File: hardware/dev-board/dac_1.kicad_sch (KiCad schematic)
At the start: 68 parts, among them IC1 ADV7393BCPZ, J2 CVBS

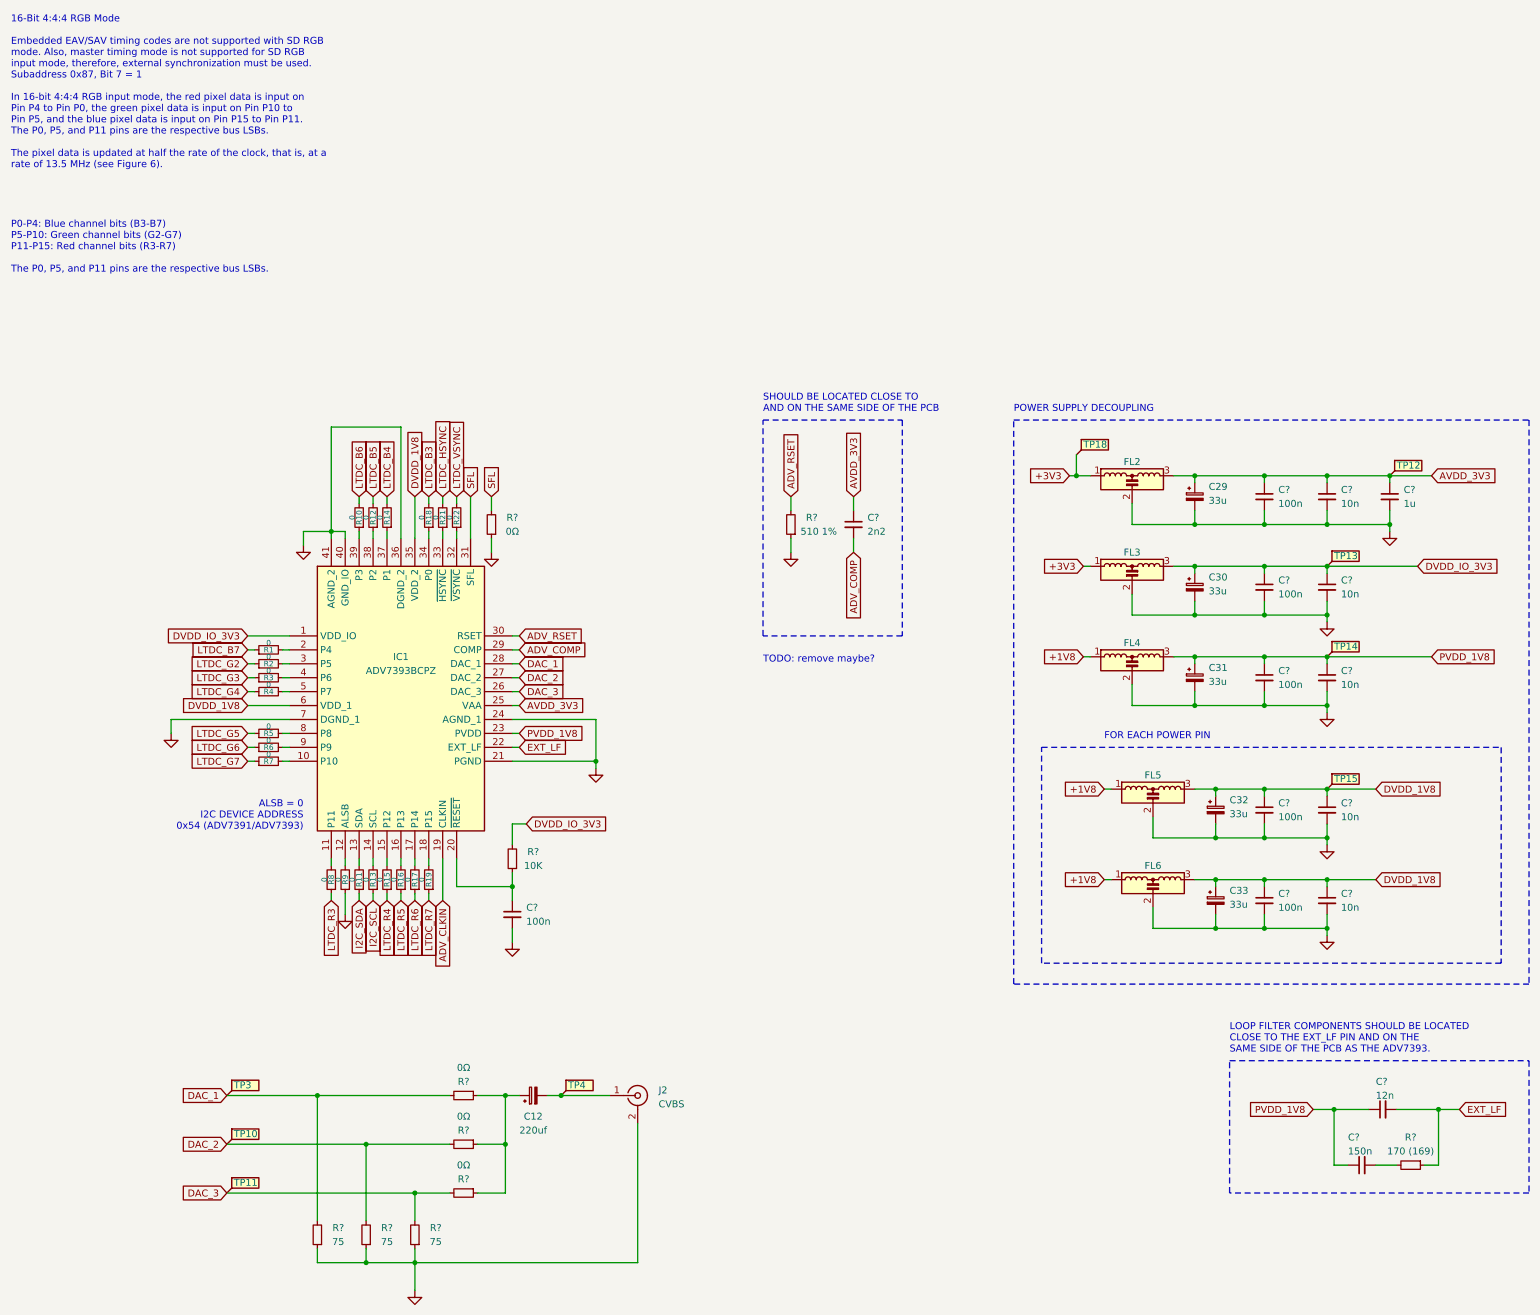
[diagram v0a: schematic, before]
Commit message: adv7393 dev-board done
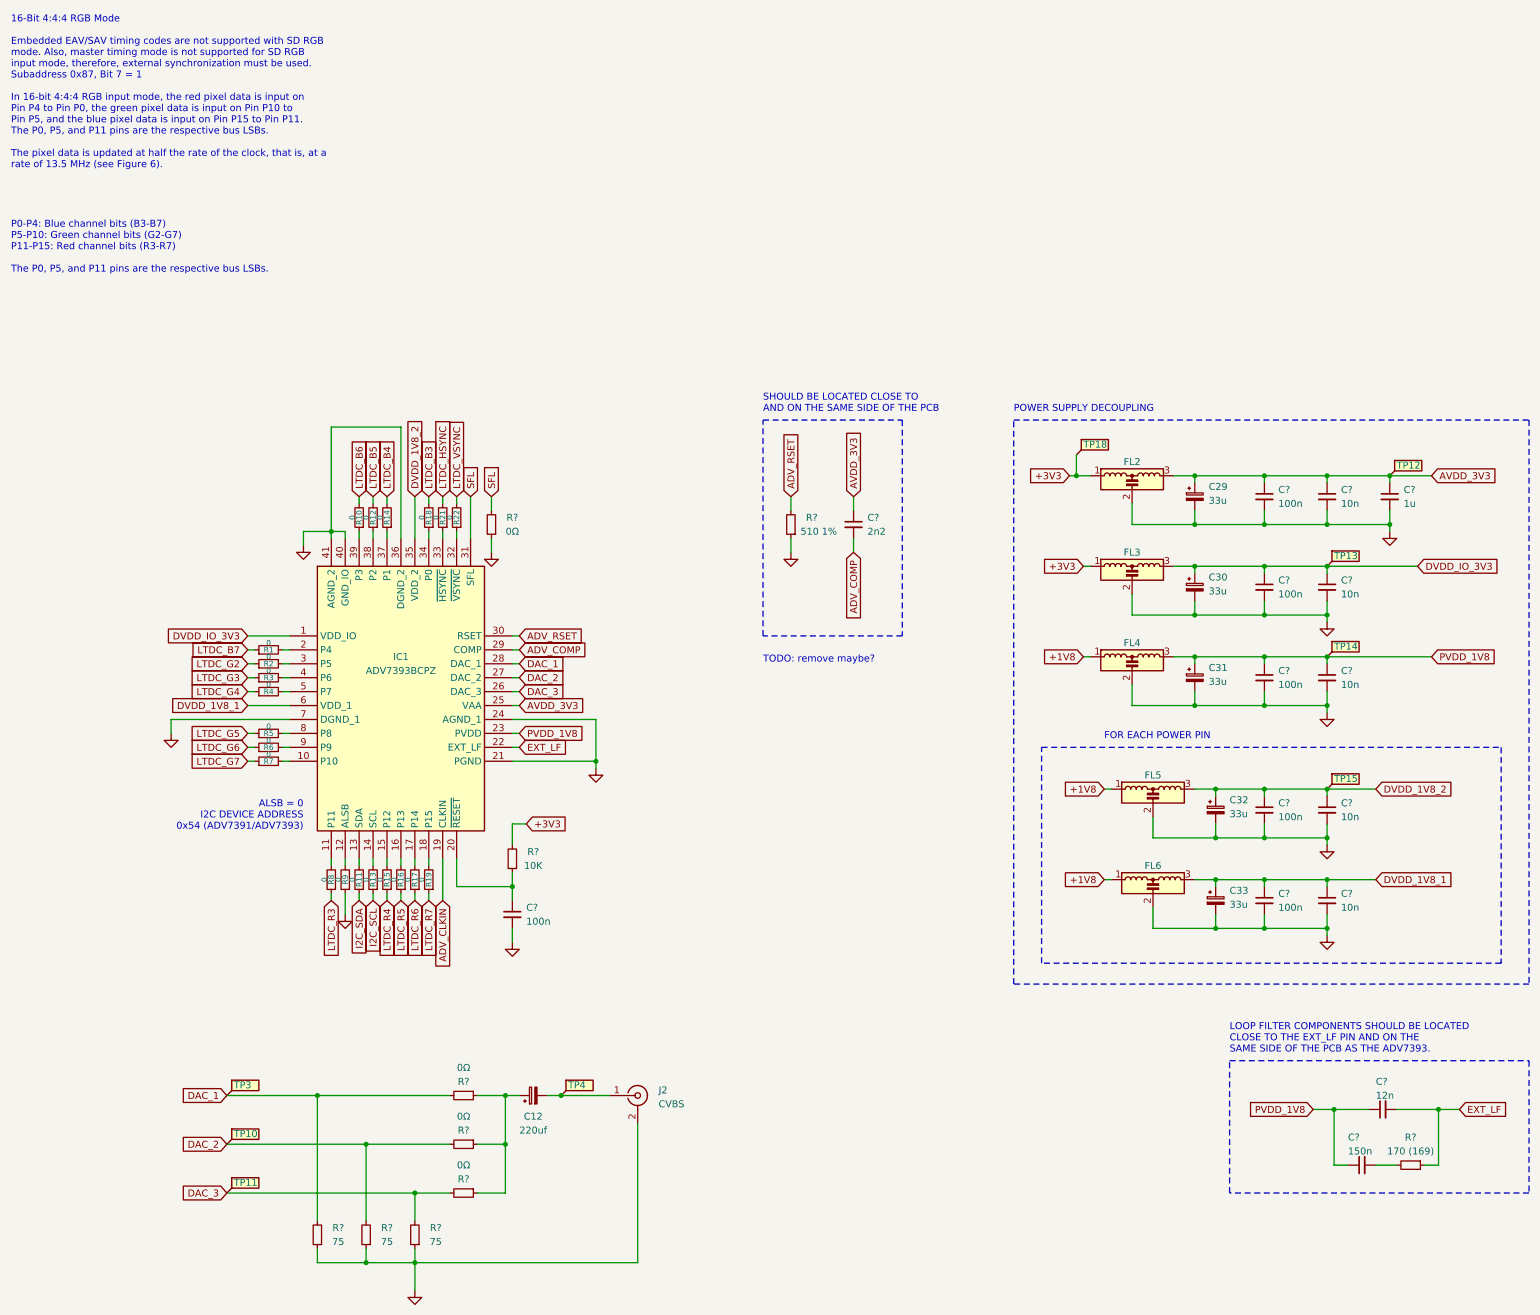
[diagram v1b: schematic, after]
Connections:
- net +3V3: now also R?.2
- net DVDD_IO_3V3: no longer R?.2
- net DVDD_1V8 renamed DVDD_1V8_2
- net DVDD_1V8_2: no longer C33.1, C?.1, C?.1, FL6.3, IC1.6 (VDD_1)
- new net DVDD_1V8_1: C33.1, C?.1, C?.1, FL6.3, IC1.6 (VDD_1)
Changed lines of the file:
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@@
     )
   )
-  (global_label "DVDD_1V8" (shape input) (at 248.92 105.41 0) (fields_autoplaced)
-    (effects (font (size 1.27 1.27)) (justify left))
-    (property "Intersheetrefs" "${INTERSHEET_REFS}" (at 261.279 105.41 0)
+  (global_label "DVDD_1V8_1" (shape input) (at 248.92 105.41 0) (fields_autoplaced)
+    (effects (font (size 1.27 1.27)) (justify left))
+    (property "Intersheetrefs" "${INTERSHEET_REFS}" (at 263.4561 105.41 0)
       (effects (font (size 1.27 1.27)) (justify left) hide)
     )
@@
     )
   )
+  (global_label "+3V3" (shape input) (at 93.98 95.25 0) (fields_autoplaced)
+    (effects (font (size 1.27 1.27)) (justify left))
+    (property "Intersheetrefs" "${INTERSHEET_REFS}" (at 102.0452 95.25 0)
+      (effects (font (size 1.27 1.27)) (justify left) hide)
+    )
+  )
   (global_label "DAC_3" (shape input) (at 92.71 71.12 0) (fields_autoplaced)
     (effects (font (size 1.27 1.27)) (justify left))
@@
     )
   )
-  (global_label "DVDD_IO_3V3" (shape input) (at 93.98 95.25 0) (fields_autoplaced)
-    (effects (font (size 1.27 1.27)) (justify left))
-    (property "Intersheetrefs" "${INTERSHEET_REFS}" (at 109.2419 95.25 0)
-      (effects (font (size 1.27 1.27)) (justify left) hide)
-    )
-  )
   (global_label "EXT_LF" (shape input) (at 264.16 147.32 0) (fields_autoplaced)
     (effects (font (size 1.27 1.27)) (justify left))
@@
     )
   )
-  (global_label "DVDD_1V8" (shape input) (at 248.92 88.9 0) (fields_autoplaced)
-    (effects (font (size 1.27 1.27)) (justify left))
-    (property "Intersheetrefs" "${INTERSHEET_REFS}" (at 261.279 88.9 0)
+  (global_label "DVDD_1V8_2" (shape input) (at 248.92 88.9 0) (fields_autoplaced)
+    (effects (font (size 1.27 1.27)) (justify left))
+    (property "Intersheetrefs" "${INTERSHEET_REFS}" (at 263.4561 88.9 0)
       (effects (font (size 1.27 1.27)) (justify left) hide)
     )
@@
     )
   )
-  (global_label "DVDD_1V8" (shape input) (at 43.18 73.66 180) (fields_autoplaced)
-    (effects (font (size 1.27 1.27)) (justify right))
-    (property "Intersheetrefs" "${INTERSHEET_REFS}" (at 30.821 73.66 0)
+  (global_label "DVDD_1V8_1" (shape input) (at 43.18 73.66 180) (fields_autoplaced)
+    (effects (font (size 1.27 1.27)) (justify right))
+    (property "Intersheetrefs" "${INTERSHEET_REFS}" (at 28.6439 73.66 0)
       (effects (font (size 1.27 1.27)) (justify right) hide)
     )
@@
     )
   )
-  (global_label "DVDD_1V8" (shape input) (at 73.66 35.56 90) (fields_autoplaced)
-    (effects (font (size 1.27 1.27)) (justify left))
-    (property "Intersheetrefs" "${INTERSHEET_REFS}" (at 73.66 23.201 90)
-      (effects (font (size 1.27 1.27)) (justify left) hide)
-    )
+  (global_label "DVDD_1V8_2" (shape input) (at 73.66 35.56 90) (fields_autoplaced)
+    (effects (font (size 1.27 1.27)) (justify left))
+    (property "Intersheetrefs" "${INTERSHEET_REFS}" (at 73.66 21.0239 90)
+      (effects (font (size 1.27 1.27)) (justify left) hide)
+    )
